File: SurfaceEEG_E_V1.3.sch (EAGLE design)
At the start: 10 parts, among them IC1 LMP7702

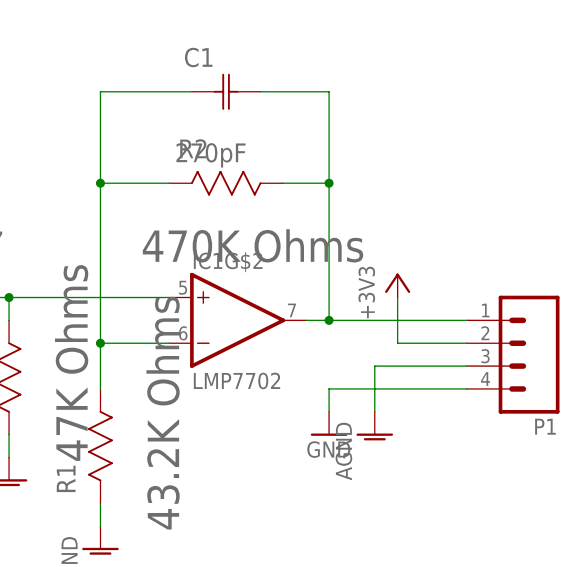
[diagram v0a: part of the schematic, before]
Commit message: Updated SurfaceEEG_E
Updated SurfaceEEG_E to V1.3. Replaced solder pads. Improved layout and
checked DRC.
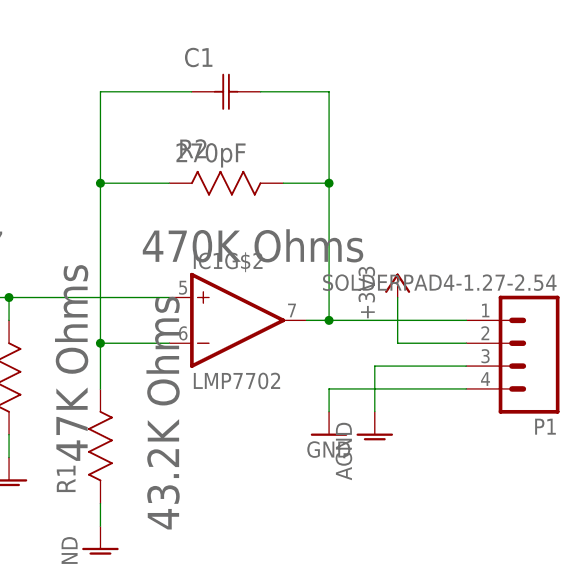
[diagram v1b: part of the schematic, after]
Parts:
- P1: value (none) -> SOLDERPAD4-1.27-2.54; device SparkFun-Connectors:M04SMD -> (custom)-new-components:SOLDERPAD4-1.27-2.54
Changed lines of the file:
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@@
 <?xml version="1.0" encoding="utf-8"?>
 <!DOCTYPE eagle SYSTEM "eagle.dtd">
-<eagle version="7.5.0">
+<eagle version="7.7.0">
 <drawing>
 <settings>
@@
 <part name="R3" library="(manufact)-resistors-YAGEO-element14" deviceset="RC0603FR-0747KL" device="" value="47K Ohms"/>
 <part name="AGND2" library="supply1" deviceset="AGND" device=""/>
-<part name="P1" library="SparkFun-Connectors" deviceset="M04" device="SMD"/>
+<part name="P1" library="(custom)-new-components" deviceset="SOLDERPAD4-1.27-2.54" device=""/>
 <part name="+3V2" library="supply1" deviceset="+3V3" device=""/>
 <part name="GND2" library="supply1" deviceset="GND" device=""/>
